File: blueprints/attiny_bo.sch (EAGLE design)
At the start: 11 parts, among them IC1 ATTiny85, J1 AVR_SPI_PRG_6NS

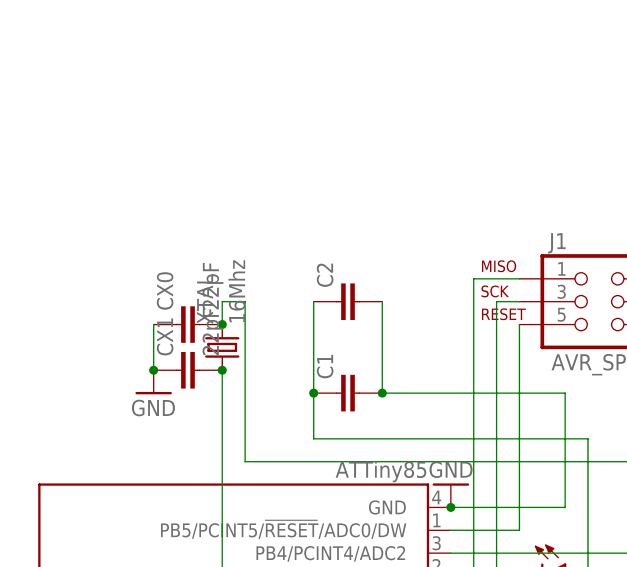
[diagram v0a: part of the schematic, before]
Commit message: switched to smaller and better available cxtal
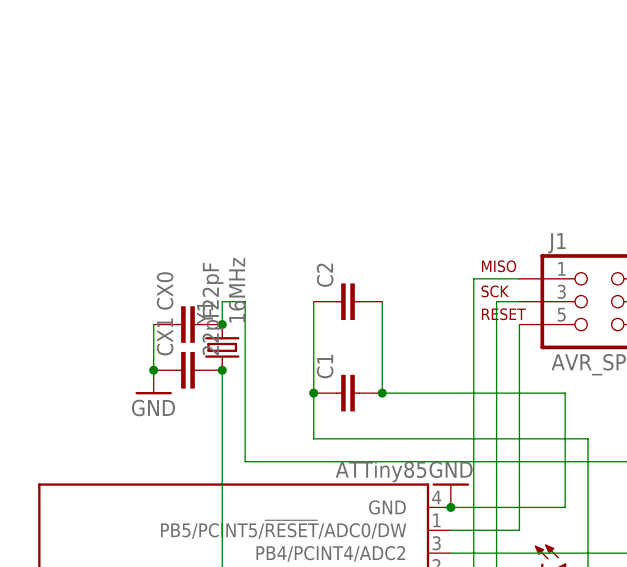
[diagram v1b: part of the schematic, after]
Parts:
- removed XTAL: 16Mhz, crystal:CRYSTALCTS406
- added Y1: 16MHz, SparkFun-FreqCtrl:CRYSTAL5X3
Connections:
- net PB3: now also Y1.1; no longer XTAL.1
- net PB4: now also Y1.2; no longer XTAL.2
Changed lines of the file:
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@@
 <part name="CX1" library="rcl" deviceset="C-EU" device="C0603" value="22pF"/>
 <part name="GND4" library="supply1" deviceset="GND" device=""/>
-<part name="XTAL" library="crystal" deviceset="CRYSTAL" device="CTS406" value="16Mhz"/>
+<part name="Y1" library="SparkFun-FreqCtrl" deviceset="CRYSTAL" device="5X3" value="16MHz"/>
 </parts>
 <sheets>
@@
 <instance part="CX1" gate="G$1" x="20.32" y="99.06" rot="R90"/>
 <instance part="GND4" gate="1" x="17.78" y="96.52"/>
-<instance part="XTAL" gate="G$1" x="25.4" y="101.6" rot="R90"/>
+<instance part="Y1" gate="G$1" x="25.4" y="101.6" rot="R90"/>
 </instances>
 <busses>
@@
 <wire x1="58.42" y1="58.42" x2="25.4" y2="58.42" width="0.1524" layer="91"/>
 <wire x1="25.4" y1="58.42" x2="25.4" y2="99.06" width="0.1524" layer="91"/>
-<pinref part="XTAL" gate="G$1" pin="1"/>
+<pinref part="Y1" gate="G$1" pin="1"/>
 <junction x="25.4" y="99.06"/>
 </segment>
@@
 <wire x1="25.4" y1="106.68" x2="25.4" y2="104.14" width="0.1524" layer="91"/>
 <junction x="71.12" y="78.74"/>
-<pinref part="XTAL" gate="G$1" pin="2"/>
+<pinref part="Y1" gate="G$1" pin="2"/>
 <junction x="25.4" y="104.14"/>
 </segment>
